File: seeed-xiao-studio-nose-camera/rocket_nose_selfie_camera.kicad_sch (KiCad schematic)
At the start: 16 parts, among them J1 LOGGER TRIGGER / STATUS, J2 UART DEBUG (3V3 TTL), U1 Seeed Studio XIAO ESP32-S3 Se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

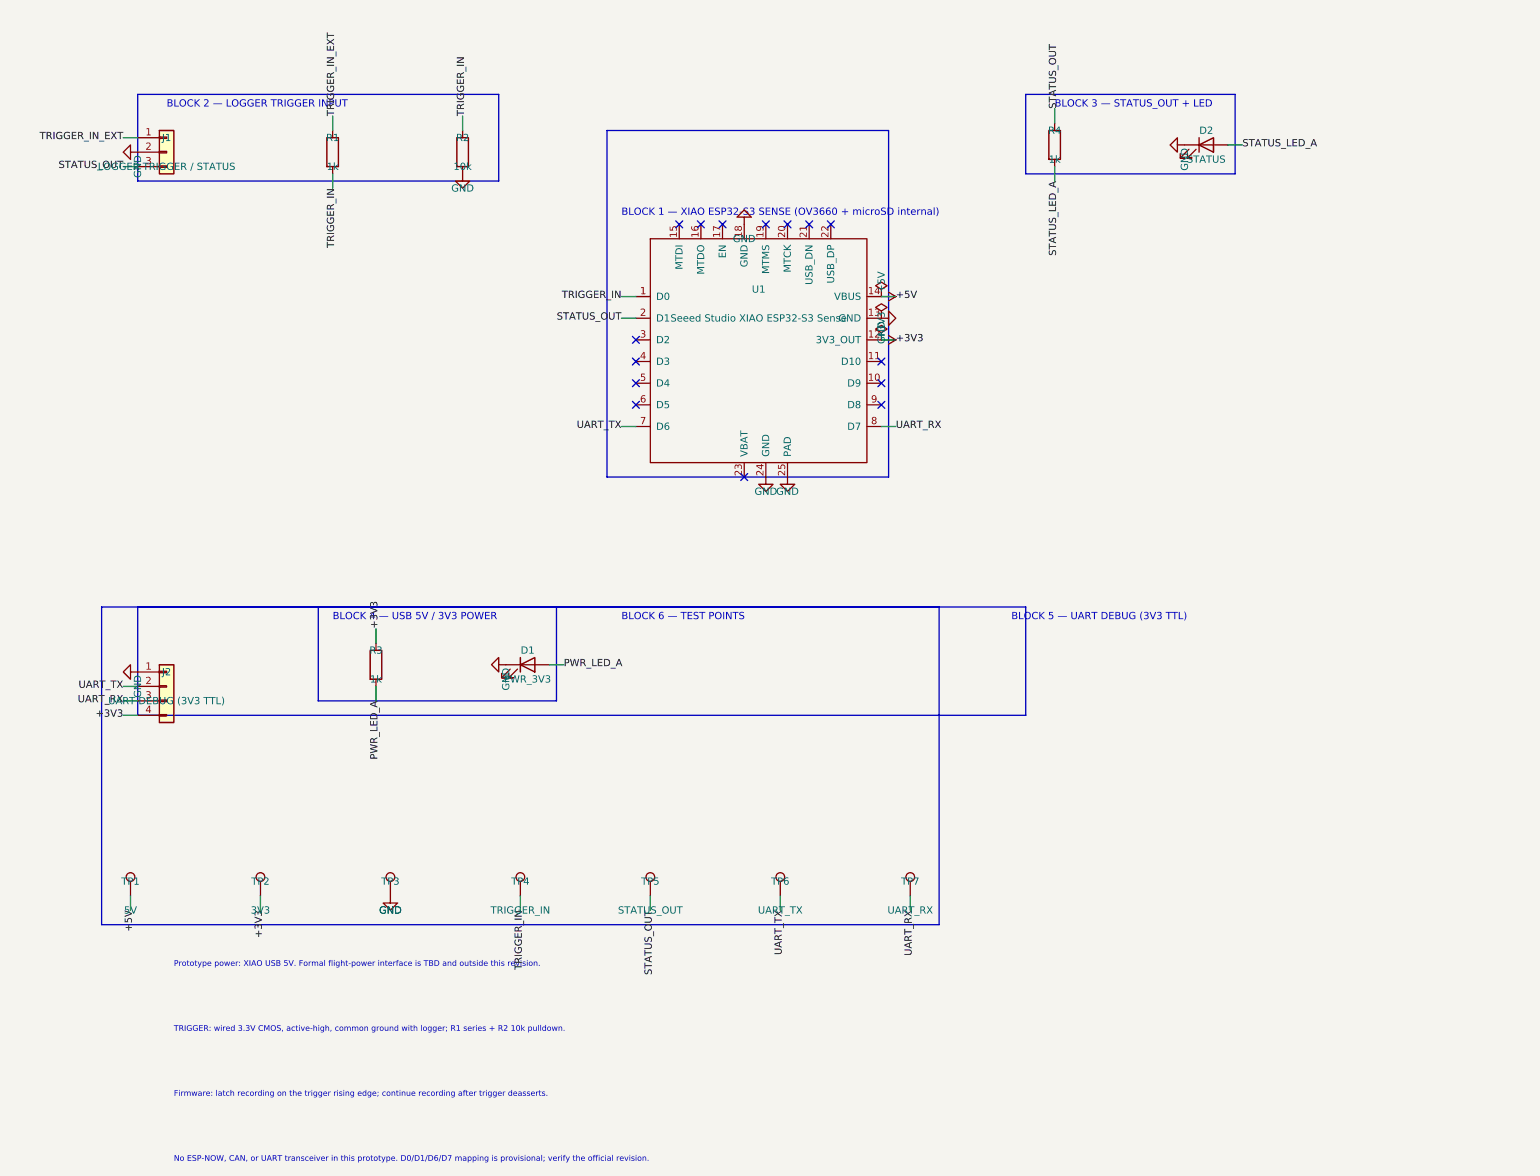
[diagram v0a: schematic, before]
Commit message: sch: add schematic symbols and topology
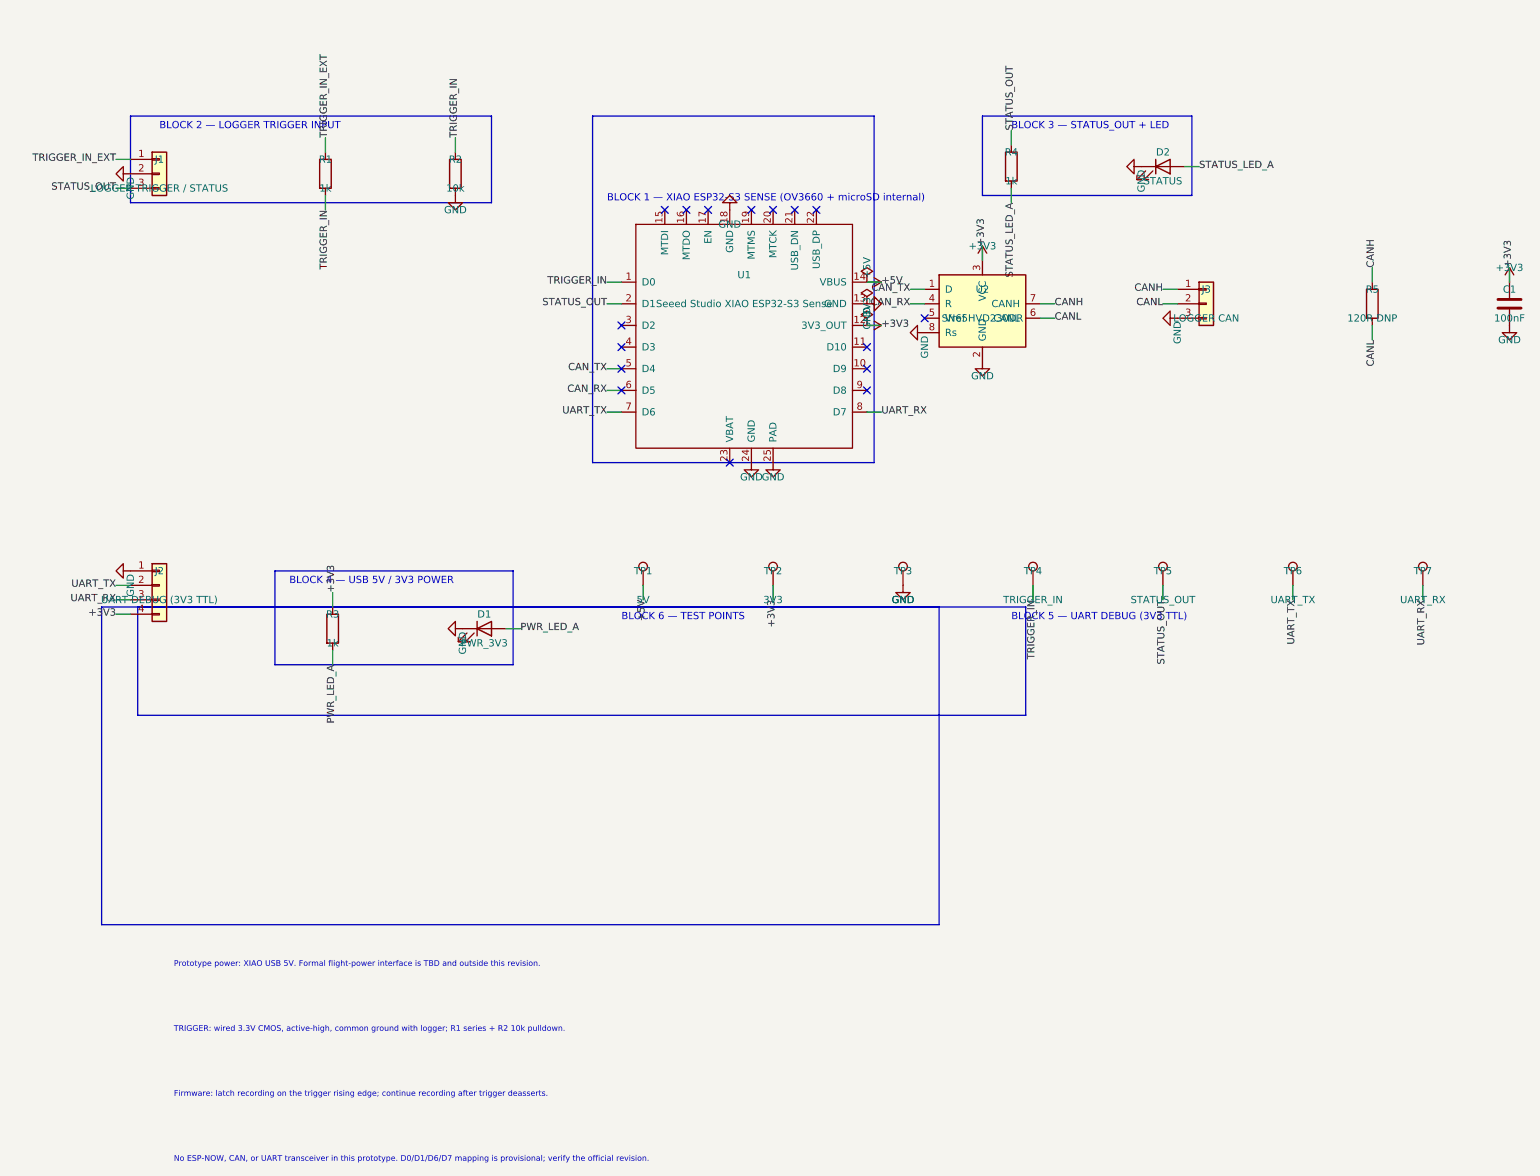
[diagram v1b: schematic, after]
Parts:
- added C1: 100nF, Capacitor_SMD:C_0603_1608Metric, symbol Device:C
- added J3: LOGGER CAN, Connector_PinHeader_2.54mm:PinHeader_1x03_P2.54mm_Vertical, symbol Connector_Generic:Conn_01x03
- added R5: 120R DNP, Resistor_SMD:R_0603_1608Metric, symbol Device:R
- added U2: SN65HVD230DR, Package_SO:SOIC-8_3.9x4.9mm_P1.27mm, symbol Interface_CAN_LIN:SN65HVD230
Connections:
- net +3V3: now also C1.1, U2.3 (VCC)
- net GND: now also C1.2, J3.3 (Pin_3), U2.2 (GND), U2.8 (Rs)
- net CAN_TX: now reaches U1.5 (D4)
- net CAN_TX: now also U2.1 (D)
- net CAN_RX: now reaches U1.6 (D5)
- net CAN_RX: now also U2.4 (R)
- new net CANH: J3.1 (Pin_1), R5.1, U2.7 (CANH)
- new net CANL: J3.2 (Pin_2), R5.2, U2.6 (CANL)
- no-connect marks 15 -> 16
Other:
- moved on the sheet: D1, D2, J1, J2, R1, R2, R3, R4, TP1, TP2, TP3, TP4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
